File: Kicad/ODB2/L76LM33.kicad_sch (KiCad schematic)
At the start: 0 parts

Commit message: edit titles
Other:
- company: (none) -> GAUL
- title: (none) -> GPS
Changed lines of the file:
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@@
 	(generator_version "8.0")
 	(paper "A4")
+	(title_block
+		(title "GPS")
+		(date "2024-11-09")
+		(company "GAUL")
+	)
 )

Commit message: add titles
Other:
- note added: "GPS"
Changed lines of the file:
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@@
 		(company "GAUL")
 	)
+	(text "GPS"
+		(exclude_from_sim no)
+		(at 22.352 18.288 0)
+		(effects
+			(font
+				(size 6 6)
+				(thickness 1.2)
+				(bold yes)
+			)
+		)
+	)
 )

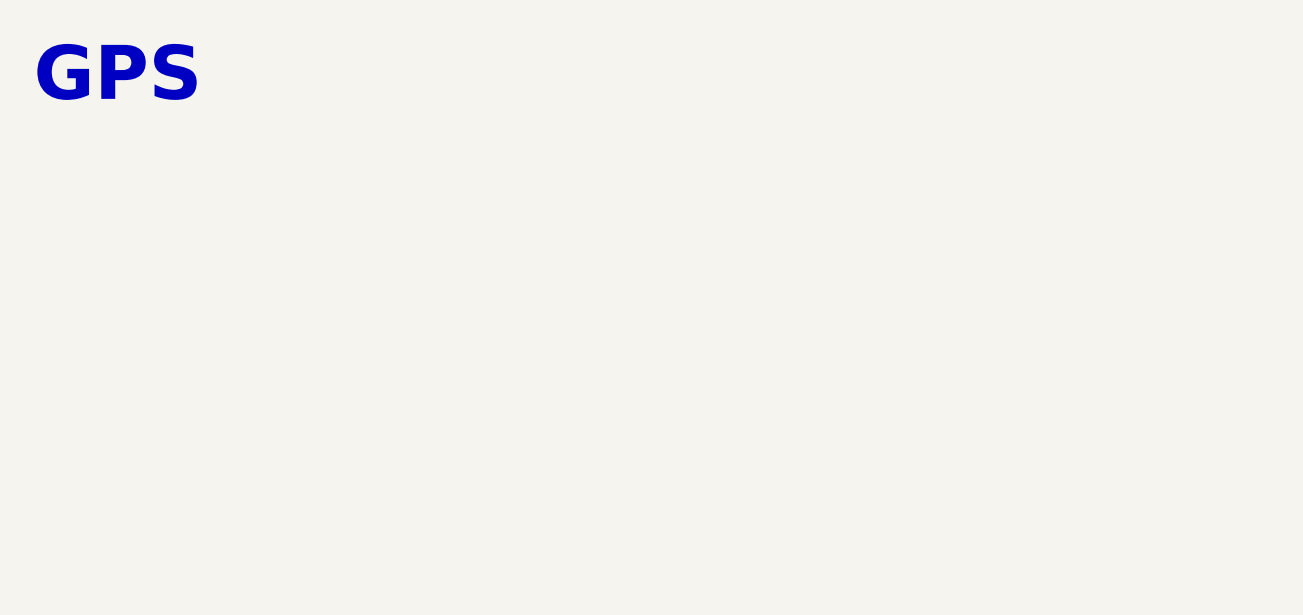
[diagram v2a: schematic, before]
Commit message: add sensors
ICM
L76L
MS580
PowerSupply
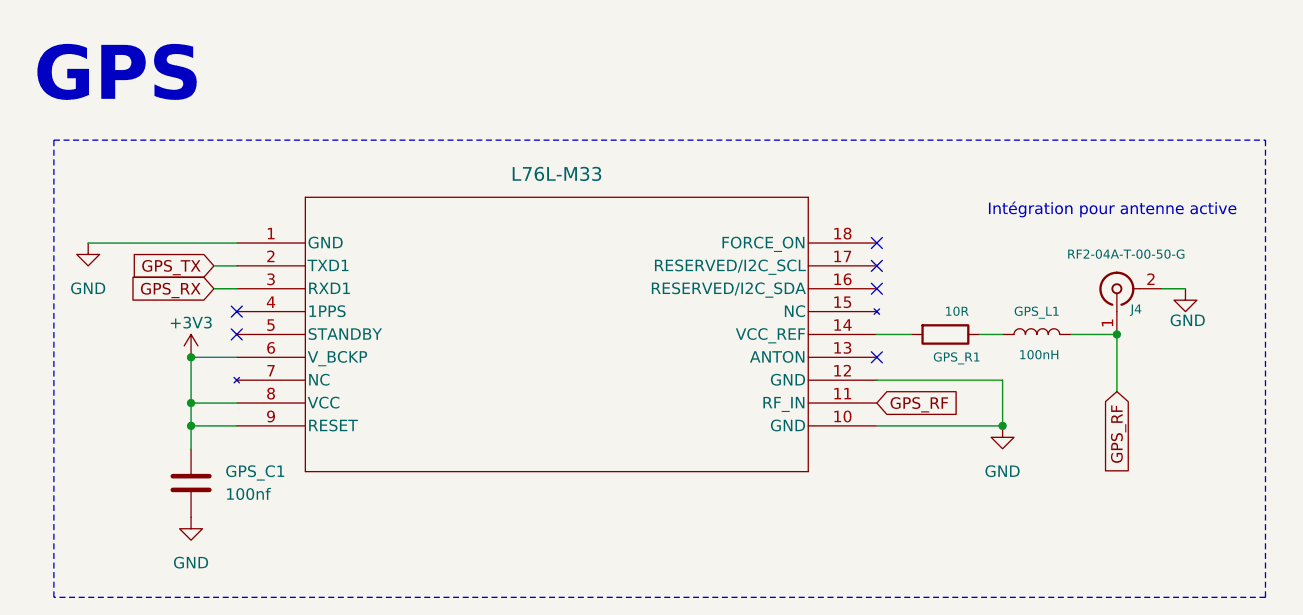
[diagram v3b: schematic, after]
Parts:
- added GPS_C1: 100nf, symbol Device:C
- added GPS_L1: 100nH, Inductor_SMD:L_0805_2012Metric, symbol Device:L
- added GPS_R1: 10R, Resistor_SMD:R_0805_2012Metric, symbol Device:R
- added J4: RF2-04A-T-00-50-G, Connector_Coaxial:SMA_Wurth_60312002114503_Vertical, symbol Connector:Conn_Coaxial
- added U5: L76L-M33, L76_QWS, symbol ODB_Lib:L76L-M33
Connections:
- new net: GPS_R1.2, U5.14 (VCC_REF)
- new net: GPS_L1.1, GPS_R1.1
- new net +3V3: GPS_C1.1, U5.6 (V_BCKP), U5.8 (VCC), U5.9 (RESET)
- new net GND: GPS_C1.2, J4.2 (Ext), U5.1 (GND), U5.10 (GND), U5.12 (GND)
- new net GPS_RF: GPS_L1.2, J4.1 (In), U5.11 (RF_IN)
- new net GPS_RX: U5.3 (RXD1)
- new net GPS_TX: U5.2 (TXD1)
- no-connect marks 0 -> 6
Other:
- note added: "Intégration pour antenne active"

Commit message: fix commit
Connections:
- net GPS_TX renamed UART1_GPS_TX
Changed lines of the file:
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@@
 		)
 	)
-	(global_label "GPS_TX"
+	(global_label "UART1_GPS_TX"
 		(shape input)
 		(at 33.02 39.37 180)
@@
 		)
 		(property "Intersheetrefs" "${INTERSHEET_REFS}"
-			(at 23.1406 39.37 0)
+			(at 16.3068 39.37 0)
 			(effects
 				(font
@@
 		(lib_id "power:GND")
 		(at 19.05 36.83 0)
-		(unit 1)
-		(exclude_from_sim no)
-		(in_bom yes)
-		(on_board yes)
-		(dnp no)
-		(fields_autoplaced yes)
+		(mirror x)
+		(unit 1)
+		(exclude_from_sim no)
+		(in_bom yes)
+		(on_board yes)
+		(dnp no)
 		(property "Reference" "#PWR048"
-			(at 19.05 43.18 0)
+			(at 19.05 30.48 0)
 			(effects
 				(font
@@
 		)
 		(property "Value" "GND"
-			(at 19.05 41.91 0)
-			(effects
-				(font
+			(at 19.05 31.75 0)
+			(effects
+				(font

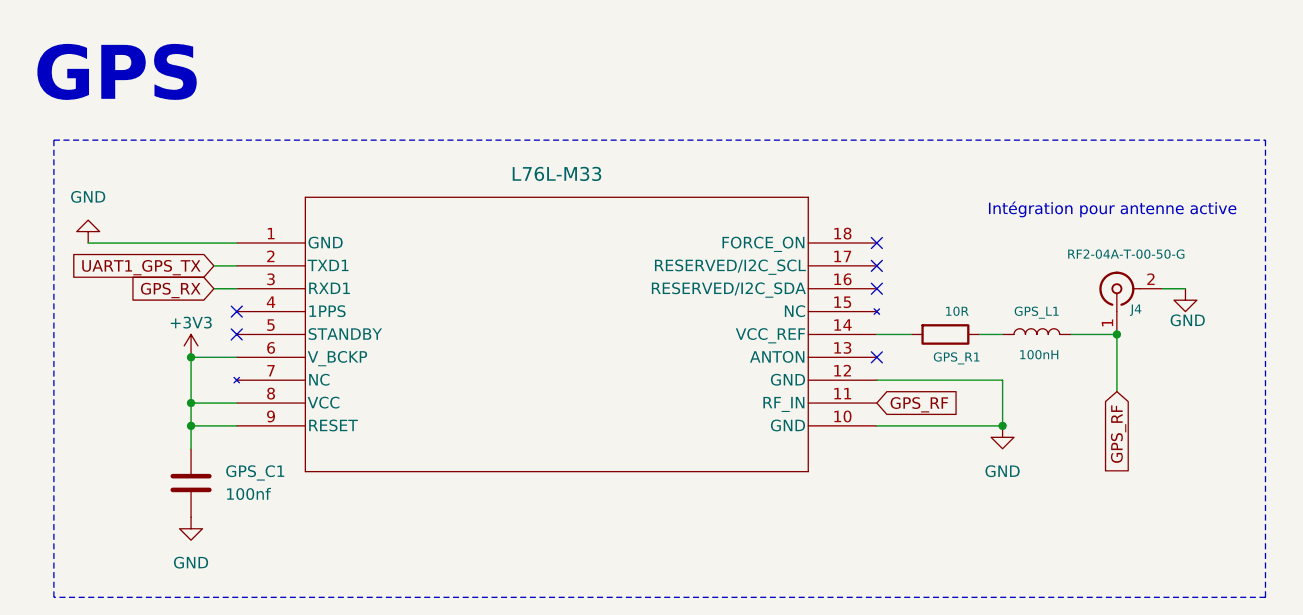
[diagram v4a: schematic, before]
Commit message: fix label
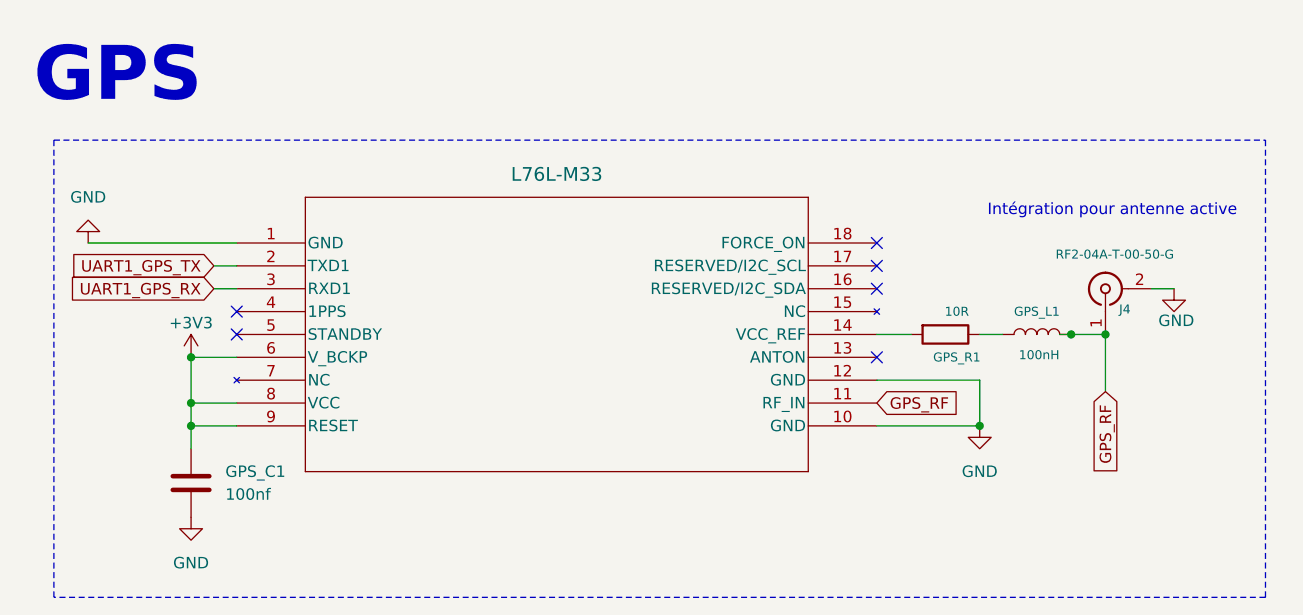
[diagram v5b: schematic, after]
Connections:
- net GPS_RX renamed UART1_GPS_RX
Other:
- moved on the sheet: J4
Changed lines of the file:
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@@
 	)
 	(junction
-		(at 133.35 46.99)
+		(at 132.08 46.99)
 		(diameter 0)
 		(color 0 0 0 0)
@@
 	)
 	(junction
-		(at 120.65 57.15)
+		(at 128.27 46.99)
 		(diameter 0)
 		(color 0 0 0 0)
 	)
+	(junction
+		(at 118.11 57.15)
+		(diameter 0)
+		(color 0 0 0 0)
+	)
 	(no_connect
 		(at 106.68 49.53)
@@
 	(wire
 		(pts
-			(xy 140.97 41.91) (xy 138.43 41.91)
+			(xy 139.7 41.91) (xy 137.16 41.91)
 		)
 		(stroke
@@
 	(wire
 		(pts
-			(xy 128.27 46.99) (xy 133.35 46.99)
+			(xy 127 46.99) (xy 128.27 46.99)
 		)
 		(stroke
@@
 	(wire
 		(pts
-			(xy 106.68 57.15) (xy 120.65 57.15)
+			(xy 106.68 57.15) (xy 118.11 57.15)
 		)
 		(stroke
@@
 	(wire
 		(pts
-			(xy 120.65 52.07) (xy 120.65 57.15)
-		)
-		(stroke
-			(width 0)
-			(type default)
-		)
-	)
-	(wire
-		(pts
-			(xy 106.68 52.07) (xy 120.65 52.07)
-		)
-		(stroke
-			(width 0)
-			(type default)
-		)
-	)
-	(wire
-		(pts
-			(xy 133.35 53.34) (xy 133.35 46.99)
+			(xy 118.11 52.07) (xy 118.11 57.15)
+		)
+		(stroke
+			(width 0)
+			(type default)
+		)
+	)
+	(wire
+		(pts
+			(xy 106.68 52.07) (xy 118.11 52.07)
+		)
+		(stroke
+			(width 0)
+			(type default)
+		)
+	)
+	(wire
+		(pts
+			(xy 132.08 53.34) (xy 132.08 46.99)
+		)
+		(stroke
+			(width 0)
+			(type default)
+		)
+	)
+	(wire
+		(pts
+			(xy 128.27 46.99) (xy 132.08 46.99)
 		)
 		(stroke
@@
 		)
 	)
-	(global_label "GPS_RX"
+	(global_label "UART1_GPS_RX"
 		(shape input)
 		(at 33.02 41.91 180)
@@
 		)
 		(property "Intersheetrefs" "${INTERSHEET_REFS}"
-			(at 22.8382 41.91 0)
+			(at 16.0044 41.91 0)
 			(effects
 				(font
@@
 	(global_label "GPS_RF"
 		(shape input)
-		(at 133.35 53.34 270)
+		(at 132.08 53.34 270)
 		(fields_autoplaced yes)
 		(effects
@@
 		)
 		(property "Intersheetrefs" "${INTERSHEET_REFS}"
-			(at 133.35 63.4009 90)
+			(at 132.08 63.4009 90)
 			(effects
 				(font
@@
 	(symbol
 		(lib_id "Connector:Conn_Coaxial")
-		(at 133.35 41.91 90)
+		(at 132.08 41.91 90)
 		(unit 1)
 		(exclude_from_sim no)
@@
 		(dnp no)
 		(property "Reference" "J4"
-			(at 136.144 44.196 90)
+			(at 134.874 44.196 90)
 			(effects
 				(font
@@
 		)
 		(property "Value" "RF2-04A-T-00-50-G"
-			(at 140.97 38.1 90)
+			(at 139.7 38.1 90)
 			(effects
 				(font
@@
 		)
 		(property "Footprint" "Connector_Coaxial:SMA_Wurth_60312002114503_Vertical"
-			(at 133.35 41.91 0)
+			(at 132.08 41.91 0)
 			(effects
 				(font
@@
 		)
 		(property "Datasheet" " ~"
-			(at 133.35 41.91 0)
+			(at 132.08 41.91 0)
 			(effects
 				(font
@@
 		)
 		(property "Description" ""
-			(at 133.35 41.91 0)
+			(at 132.08 41.91 0)
 			(effects
 				(font
@@
 	(symbol
 		(lib_id "power:GND")
-		(at 140.97 41.91 0)
+		(at 139.7 41.91 0)
 		(unit 1)
 		(exclude_from_sim no)
@@
 		(dnp no)
 		(property "Reference" "#PWR052"
-			(at 140.97 48.26 0)
+			(at 139.7 48.26 0)
 			(effects
 				(font
@@
 		)
 		(property "Value" "GND"
-			(at 141.224 45.466 0)
+			(at 139.954 45.466 0)
 			(effects
 				(font
@@
 		)
 		(property "Footprint" ""
-			(at 140.97 41.91 0)
+			(at 139.7 41.91 0)
 			(effects
 				(font
@@
 		)
 		(property "Datasheet" ""
-			(at 140.97 41.91 0)
+			(at 139.7 41.91 0)
 			(effects
 				(font
@@
 		)
 		(property "Description" "Power symbol creates a global label with name \"GND\" , ground"
-			(at 140.97 41.91 0)
+			(at 139.7 41.91 0)
 			(effects
 				(font
@@
 	(symbol
 		(lib_id "power:GND")
-		(at 120.65 57.15 0)
+		(at 118.11 57.15 0)
 		(unit 1)
 		(exclude_from_sim no)
@@
 		(fields_autoplaced yes)
 		(property "Reference" "#PWR051"
-			(at 120.65 63.5 0)
+			(at 118.11 63.5 0)
 			(effects
 				(font
@@
 		)
 		(property "Value" "GND"
-			(at 120.65 62.23 0)
+			(at 118.11 62.23 0)
 			(effects
 				(font
@@
 		)
 		(property "Footprint" ""
-			(at 120.65 57.15 0)
+			(at 118.11 57.15 0)
 			(effects
 				(font
@@
 		)
 		(property "Datasheet" ""
-			(at 120.65 57.15 0)
+			(at 118.11 57.15 0)
 			(effects
 				(font
@@
 		)
 		(property "Description" "Power symbol creates a global label with name \"GND\" , ground"
-			(at 120.65 57.15 0)
-			(effects
-				(font
+			(at 118.11 57.15 0)
+			(effects
+				(font

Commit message: merge all sensors to main page + fix NC
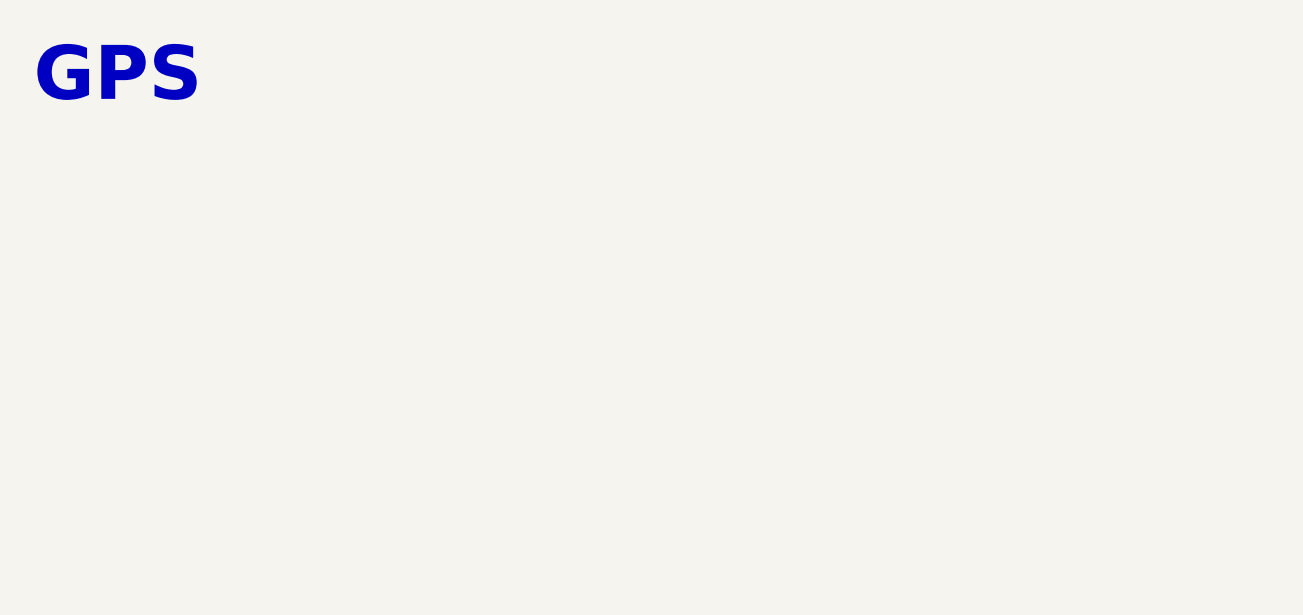
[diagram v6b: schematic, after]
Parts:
- removed GPS_C1: 100nf, symbol Device:C
- removed GPS_L1: 100nH, Inductor_SMD:L_0805_2012Metric, symbol Device:L
- removed GPS_R1: 10R, Resistor_SMD:R_0805_2012Metric, symbol Device:R
- removed J4: RF2-04A-T-00-50-G, Connector_Coaxial:SMA_Wurth_60312002114503_Vertical, symbol Connector:Conn_Coaxial
- removed U5: L76L-M33, L76_QWS, symbol ODB_Lib:L76L-M33
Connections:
- no-connect marks 6 -> 0
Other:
- note removed: "Intégration pour antenne active"
